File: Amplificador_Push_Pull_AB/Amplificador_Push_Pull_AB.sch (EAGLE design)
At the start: 51 parts, among them IC1 LM741P, IC3 788TV, P2 10k, Q1 BC547, Q10 TIP42C, Q2 BC547, Q4 BC547, Q7 BC547, Q8 BC547, T2 2SC1307

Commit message: Separate fround line done. Its resistance is approximately 0.1 ohm. Schematic connections integrity verified. Check DRC next time!
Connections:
- net N$24 renamed +5V
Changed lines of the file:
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@@
 </segment>
 </net>
-<net name="N$24" class="0">
+<net name="+5V" class="0">
 <segment>
 <pinref part="RMIC" gate="G$1" pin="1"/>

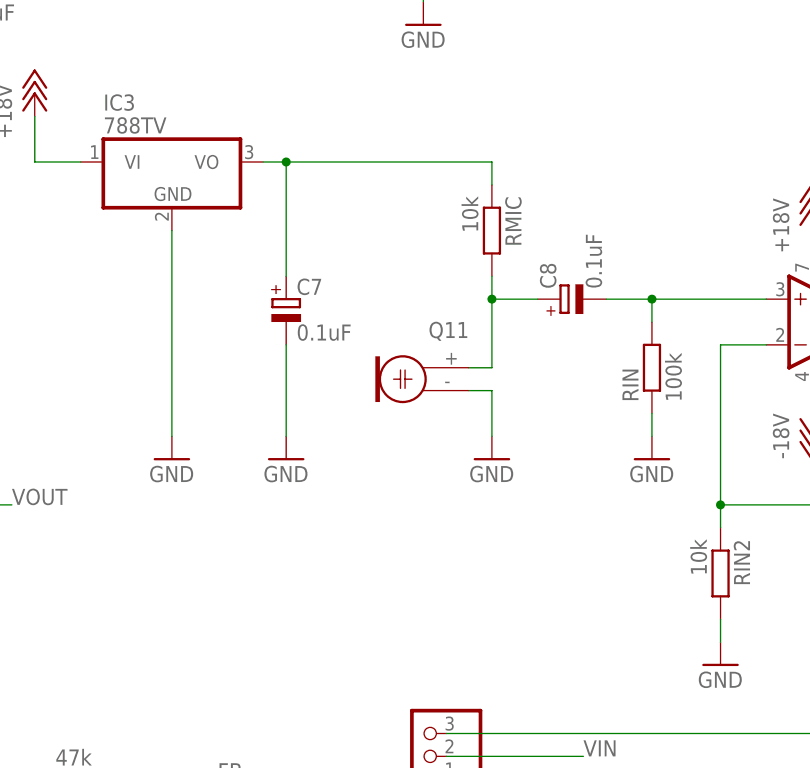
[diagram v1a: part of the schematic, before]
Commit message: Led added on schematic. Need to put allocate it in board now.
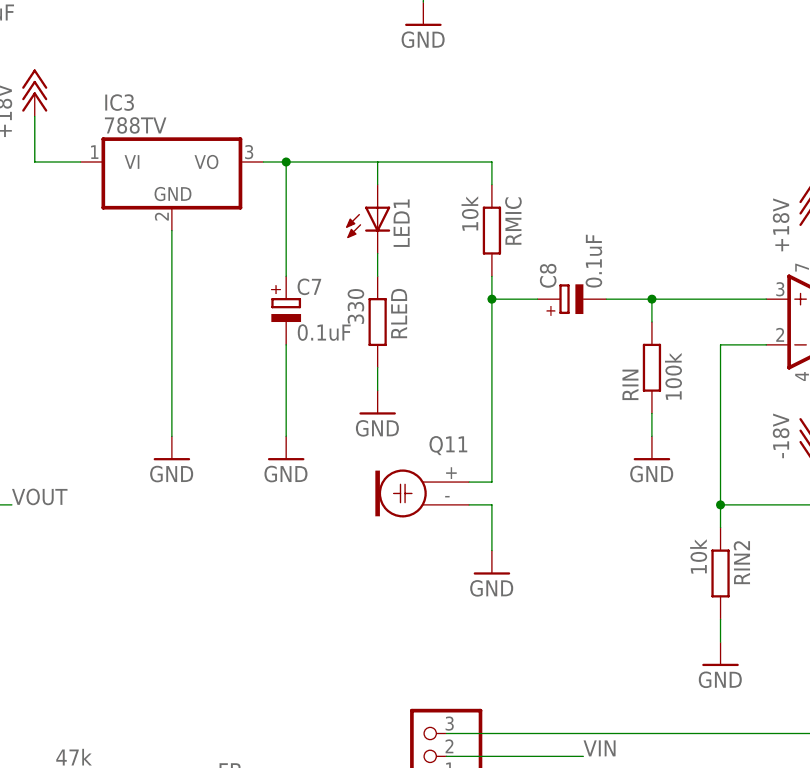
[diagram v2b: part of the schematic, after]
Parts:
- added LED1: (no value), adafruit:LED5MM
- added RLED: 330, rcl:R-EU_0207/10
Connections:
- new net N$18: LED1.C, RLED.1
- net +5V: now also LED1.A
- net GND: now also RLED.2
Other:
- moved on the sheet: Q11
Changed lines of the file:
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@@
 <part name="RLEFT" library="rcl" deviceset="R-EU_" device="0207/7" value="10k"/>
 <part name="IC3" library="linear" deviceset="78*" device="TV" technology="8"/>
+<part name="LED1" library="adafruit" deviceset="LED" device="5MM"/>
+<part name="RLED" library="rcl" deviceset="R-EU_" device="0207/10" value="330"/>
+<part name="GND6" library="supply1" deviceset="GND" device=""/>
 </parts>
 <sheets>
@@
 <instance part="RRIGHT" gate="G$1" x="200.66" y="-12.7" rot="MR180"/>
 <instance part="RMIC" gate="G$1" x="172.72" y="76.2" rot="R270"/>
-<instance part="GND9" gate="1" x="172.72" y="50.8"/>
+<instance part="GND9" gate="1" x="172.72" y="38.1"/>
 <instance part="IC1" gate="A" x="210.82" y="66.04"/>
 <instance part="P+4" gate="1" x="208.28" y="78.74"/>
 <instance part="P-4" gate="1" x="208.28" y="53.34"/>
 <instance part="P1" gate="G$1" x="66.04" y="55.88"/>
-<instance part="Q11" gate="G$1" x="165.1" y="58.42" rot="R180"/>
+<instance part="Q11" gate="G$1" x="165.1" y="45.72" rot="R180"/>
 <instance part="P+5" gate="1" x="121.92" y="91.44"/>
 <instance part="GND10" gate="1" x="137.16" y="50.8"/>
@@
 <instance part="RLEFT" gate="G$1" x="200.66" y="-2.54" rot="MR180"/>
 <instance part="IC3" gate="A1" x="137.16" y="83.82"/>
+<instance part="LED1" gate="G$1" x="160.02" y="78.74"/>
+<instance part="RLED" gate="G$1" x="160.02" y="66.04" rot="R270"/>
+<instance part="GND6" gate="1" x="160.02" y="55.88"/>
 </instances>
 <busses>
@@
 </segment>
 <segment>
-<wire x1="172.72" y1="58.42" x2="172.72" y2="53.34" width="0.1524" layer="91"/>
+<wire x1="172.72" y1="45.72" x2="172.72" y2="40.64" width="0.1524" layer="91"/>
 <pinref part="GND9" gate="1" pin="GND"/>
 <pinref part="Q11" gate="G$1" pin="1"/>
-<wire x1="170.18" y1="58.42" x2="172.72" y2="58.42" width="0.1524" layer="91"/>
+<wire x1="170.18" y1="45.72" x2="172.72" y2="45.72" width="0.1524" layer="91"/>
 </segment>
 <segment>
@@
 <pinref part="P2" gate="G$1" pin="A"/>
 <wire x1="233.68" y1="43.18" x2="233.68" y2="48.26" width="0.1524" layer="91"/>
+</segment>
+<segment>
+<pinref part="RLED" gate="G$1" pin="2"/>
+<wire x1="160.02" y1="60.96" x2="160.02" y2="58.42" width="0.1524" layer="91"/>
+<pinref part="GND6" gate="1" pin="GND"/>
 </segment>
 </net>
@@
 <wire x1="172.72" y1="71.12" x2="172.72" y2="68.58" width="0.1524" layer="91"/>
 <pinref part="Q11" gate="G$1" pin="2"/>
-<wire x1="172.72" y1="68.58" x2="172.72" y2="60.96" width="0.1524" layer="91"/>
-<wire x1="170.18" y1="60.96" x2="172.72" y2="60.96" width="0.1524" layer="91"/>
+<wire x1="172.72" y1="68.58" x2="172.72" y2="48.26" width="0.1524" layer="91"/>
+<wire x1="170.18" y1="48.26" x2="172.72" y2="48.26" width="0.1524" layer="91"/>
 <pinref part="C8" gate="G$1" pin="+"/>
 <wire x1="177.8" y1="68.58" x2="172.72" y2="68.58" width="0.1524" layer="91"/>
@@
 <wire x1="172.72" y1="81.28" x2="172.72" y2="83.82" width="0.1524" layer="91"/>
 <pinref part="C7" gate="G$1" pin="+"/>
-<wire x1="149.86" y1="83.82" x2="172.72" y2="83.82" width="0.1524" layer="91"/>
+<wire x1="149.86" y1="83.82" x2="160.02" y2="83.82" width="0.1524" layer="91"/>
+<wire x1="160.02" y1="83.82" x2="172.72" y2="83.82" width="0.1524" layer="91"/>
 <wire x1="149.86" y1="71.12" x2="149.86" y2="83.82" width="0.1524" layer="91"/>
 <pinref part="IC3" gate="A1" pin="VO"/>
 <wire x1="147.32" y1="83.82" x2="149.86" y2="83.82" width="0.1524" layer="91"/>
 <junction x="149.86" y="83.82"/>
+<pinref part="LED1" gate="G$1" pin="A"/>
+<wire x1="160.02" y1="81.28" x2="160.02" y2="83.82" width="0.1524" layer="91"/>
 </segment>
 </net>
@@
 </segment>
 </net>
+<net name="N$18" class="0">
+<segment>
+<pinref part="LED1" gate="G$1" pin="C"/>
+<wire x1="160.02" y1="73.66" x2="160.02" y2="71.12" width="0.1524" layer="91"/>
+<pinref part="RLED" gate="G$1" pin="1"/>
+</segment>
+</net>

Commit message: Separete ground line with polygon done. LED and its resistor added.
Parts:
- RLED, RMIC: device rcl:R-EU_0207/10 -> rcl:R-EU_0207/7
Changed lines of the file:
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@@
 <part name="GND8" library="supply1" deviceset="GND" device=""/>
 <part name="RRIGHT" library="rcl" deviceset="R-EU_" device="0207/7" value="10k"/>
-<part name="RMIC" library="rcl" deviceset="R-EU_" device="0207/10" value="10k"/>
+<part name="RMIC" library="rcl" deviceset="R-EU_" device="0207/7" value="10k"/>
 <part name="GND9" library="supply1" deviceset="GND" device=""/>
 <part name="IC1" library="linear" deviceset="*741" device="P" technology="LM"/>
@@
 <part name="IC3" library="linear" deviceset="78*" device="TV" technology="8"/>
 <part name="LED1" library="adafruit" deviceset="LED" device="5MM"/>
-<part name="RLED" library="rcl" deviceset="R-EU_" device="0207/10" value="330"/>
+<part name="RLED" library="rcl" deviceset="R-EU_" device="0207/7" value="330"/>
 <part name="GND6" library="supply1" deviceset="GND" device=""/>
 </parts>

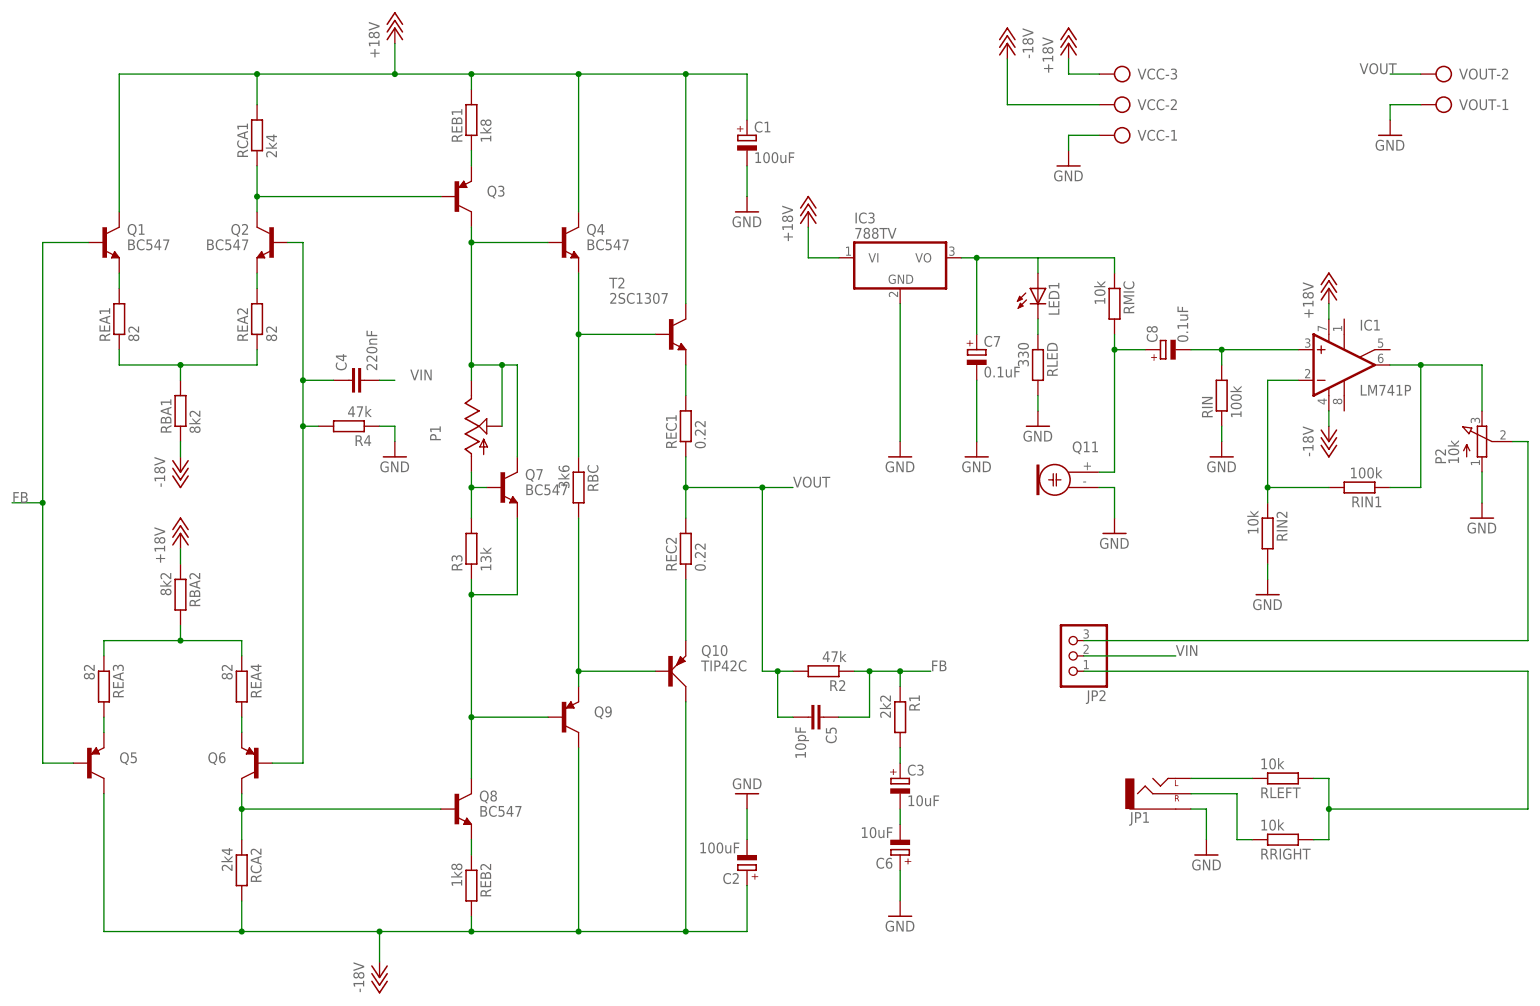
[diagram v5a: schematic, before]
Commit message: Inversed polarity capactitor problem solved. Simulation files added. PCB assembled and worked good! Next time: Limit the outputs's maximum voltage of the op. amp. through a smaller gain or decrease the potentiometer range; Also, swap the pin header used in channel selection for HH key bought.
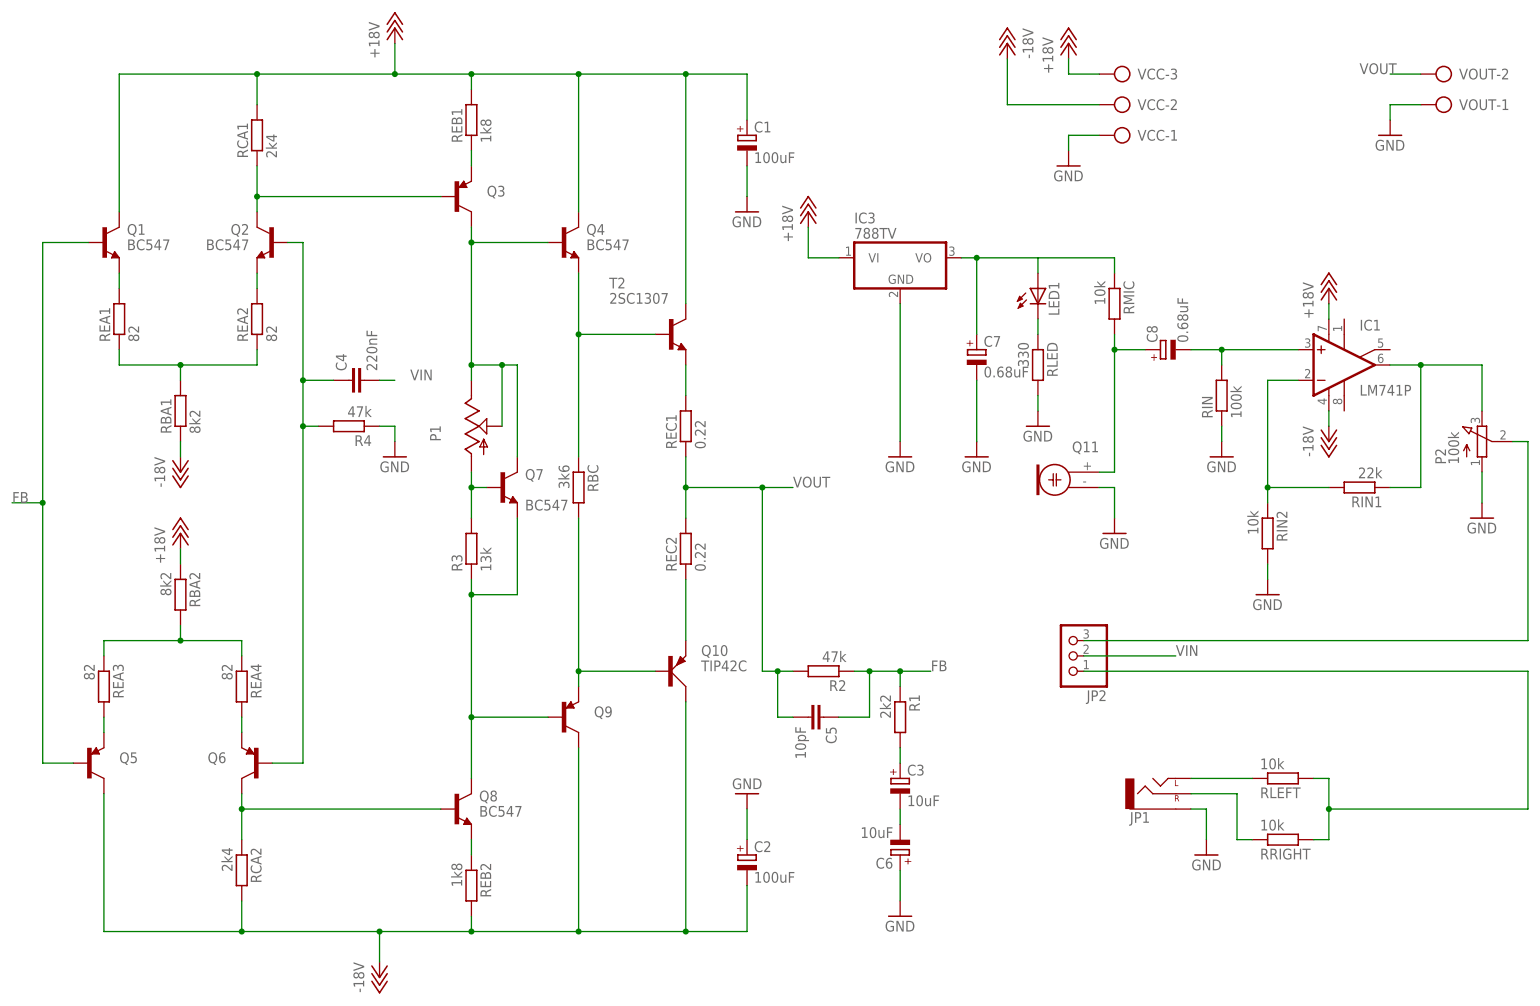
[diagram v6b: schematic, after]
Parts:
- C7, C8: value 0.1uF -> 0.68uF
- P2: value 10k -> 100k
- RIN1: value 100k -> 22k
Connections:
- net -18V: now also C2.-; no longer C2.+
- net GND: now also C2.+; no longer C2.-
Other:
- moved on the sheet: C2
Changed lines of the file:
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@@
 <part name="GND10" library="supply1" deviceset="GND" device=""/>
 <part name="C6" library="rcl" deviceset="CPOL-EU" device="E2.5-5" value="10uF"/>
-<part name="C7" library="rcl" deviceset="CPOL-EU" device="E2.5-5" value="0.1uF"/>
+<part name="C7" library="rcl" deviceset="CPOL-EU" device="E2.5-5" value="0.68uF"/>
 <part name="GND11" library="supply1" deviceset="GND" device=""/>
-<part name="C8" library="rcl" deviceset="CPOL-EU" device="E2.5-5" value="0.1uF"/>
+<part name="C8" library="rcl" deviceset="CPOL-EU" device="E2.5-5" value="0.68uF"/>
 <part name="RIN" library="rcl" deviceset="R-EU_" device="0207/7" value="100k"/>
 <part name="GND12" library="supply1" deviceset="GND" device=""/>
-<part name="RIN1" library="rcl" deviceset="R-EU_" device="0207/7" value="100k"/>
+<part name="RIN1" library="rcl" deviceset="R-EU_" device="0207/7" value="22k"/>
 <part name="RIN2" library="rcl" deviceset="R-EU_" device="0207/10" value="10k"/>
 <part name="GND13" library="supply1" deviceset="GND" device=""/>
-<part name="P2" library="pot" deviceset="3RP/1610N" device="" value="10k"/>
+<part name="P2" library="pot" deviceset="3RP/1610N" device="" value="100k"/>
 <part name="JP2" library="pinhead" deviceset="PINHD-1X3" device=""/>
 <part name="GND14" library="supply1" deviceset="GND" device=""/>
@@
 <instance part="P+2" gate="1" x="17.78" y="38.1"/>
 <instance part="C1" gate="G$1" x="111.76" y="104.14"/>
-<instance part="C2" gate="G$1" x="111.76" y="-17.78" rot="R180"/>
+<instance part="C2" gate="G$1" x="111.76" y="-15.24"/>
 <instance part="GND2" gate="1" x="111.76" y="91.44"/>
 <instance part="GND3" gate="1" x="111.76" y="-5.08" rot="R180"/>
@@
 <attribute name="CREVISION" x="209.52" y="-44.55" size="2.54" layer="94" font="vector"/>
 </instance>
-<instance part="Q7" gate="G$1" x="71.12" y="45.72"/>
+<instance part="Q7" gate="G$1" x="71.12" y="45.72" smashed="yes">
+<attribute name="NAME" x="74.93" y="46.99" size="1.778" layer="95"/>
+<attribute name="VALUE" x="74.93" y="41.91" size="1.778" layer="96"/>
+</instance>
 <instance part="Q3" gate="G$1" x="63.5" y="93.98"/>
 <instance part="Q4" gate="G$1" x="81.28" y="86.36"/>
@@
 </segment>
 <segment>
-<pinref part="C2" gate="G$1" pin="-"/>
-<pinref part="GND3" gate="1" pin="GND"/>
-<wire x1="111.76" y1="-12.7" x2="111.76" y2="-7.62" width="0.1524" layer="91"/>
-</segment>
-<segment>
 <pinref part="VOUT" gate="-1" pin="KL"/>
 <wire x1="223.52" y1="109.22" x2="218.44" y2="109.22" width="0.1524" layer="91"/>
@@
 <wire x1="160.02" y1="60.96" x2="160.02" y2="58.42" width="0.1524" layer="91"/>
 <pinref part="GND6" gate="1" pin="GND"/>
+</segment>
+<segment>
+<pinref part="C2" gate="G$1" pin="+"/>
+<pinref part="GND3" gate="1" pin="GND"/>
+<wire x1="111.76" y1="-12.7" x2="111.76" y2="-7.62" width="0.1524" layer="91"/>
 </segment>
 </net>
@@
 <pinref part="P-1" gate="1" pin="-18V"/>
 <wire x1="50.8" y1="-33.02" x2="50.8" y2="-27.94" width="0.1524" layer="91"/>
-<pinref part="C2" gate="G$1" pin="+"/>
-<wire x1="111.76" y1="-20.32" x2="111.76" y2="-27.94" width="0.1524" layer="91"/>
 <wire x1="111.76" y1="-27.94" x2="101.6" y2="-27.94" width="0.1524" layer="91"/>
 <junction x="101.6" y="-27.94"/>
@@
 <junction x="50.8" y="-27.94"/>
 <pinref part="Q9" gate="G$1" pin="C"/>
-</segment>
-<segment>
+<pinref part="C2" gate="G$1" pin="-"/>
+<wire x1="111.76" y1="-20.32" x2="111.76" y2="-27.94" width="0.1524" layer="91"/>
+</segment>
+<segment>
